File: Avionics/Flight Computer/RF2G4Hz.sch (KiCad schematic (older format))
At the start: 37 parts, among them J5 0734120110, U3 CC2650F128RGZR, U4 CC2592RGVR, Y5 XRCGB24M000F2P00R0

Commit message: Some more pin swapping and routing of signals. Placed reset pullup resistors.
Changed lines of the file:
@@
 $EndComp
 $Comp
-L GND #PWR063
+L GND #PWR76
 U 1 1 58AA6B6F
 P 7100 2700
-F 0 "#PWR063" H 7100 2450 50  0001 C CNN
+F 0 "#PWR76" H 7100 2450 50  0001 C CNN
 F 1 "GND" H 7100 2550 50  0000 C CNN
 F 2 "" H 7100 2700 50  0001 C CNN
@@
 $EndComp
 $Comp
-L GND #PWR064
+L GND #PWR80
 U 1 1 58AA6B99
 P 7900 2700
-F 0 "#PWR064" H 7900 2450 50  0001 C CNN
+F 0 "#PWR80" H 7900 2450 50  0001 C CNN
 F 1 "GND" H 7900 2550 50  0000 C CNN
 F 2 "" H 7900 2700 50  0001 C CNN
@@
 $EndComp
 $Comp
-L GND #PWR065
+L GND #PWR84
 U 1 1 58AA6BBC
 P 8400 2700
-F 0 "#PWR065" H 8400 2450 50  0001 C CNN
+F 0 "#PWR84" H 8400 2450 50  0001 C CNN
 F 1 "GND" H 8400 2550 50  0000 C CNN
 F 2 "" H 8400 2700 50  0001 C CNN
@@
 $EndComp
 $Comp
-L GND #PWR066
+L GND #PWR74
 U 1 1 58AA6BDF
 P 6400 1200
-F 0 "#PWR066" H 6400 950 50  0001 C CNN
+F 0 "#PWR74" H 6400 950 50  0001 C CNN
 F 1 "GND" H 6400 1050 50  0000 C CNN
 F 2 "" H 6400 1200 50  0001 C CNN
@@
 $EndComp
 $Comp
-L GND #PWR067
+L GND #PWR88
 U 1 1 58AA6E83
 P 9750 2500
-F 0 "#PWR067" H 9750 2250 50  0001 C CNN
+F 0 "#PWR88" H 9750 2250 50  0001 C CNN
 F 1 "GND" H 9750 2350 50  0000 C CNN
 F 2 "" H 9750 2500 50  0001 C CNN
@@
 $EndComp
 $Comp
-L GND #PWR068
+L GND #PWR83
 U 1 1 58AB3920
 P 8400 1750
-F 0 "#PWR068" H 8400 1500 50  0001 C CNN
+F 0 "#PWR83" H 8400 1500 50  0001 C CNN
 F 1 "GND" H 8400 1600 50  0000 C CNN
 F 2 "" H 8400 1750 50  0001 C CNN
@@
 RF Shield
 $Comp
-L GND #PWR069
+L GND #PWR75
 U 1 1 58AB48CB
 P 6750 1200
-F 0 "#PWR069" H 6750 950 50  0001 C CNN
+F 0 "#PWR75" H 6750 950 50  0001 C CNN
 F 1 "GND" H 6750 1050 50  0000 C CNN
 F 2 "" H 6750 1200 50  0001 C CNN
@@
 $EndComp
 $Comp
-L GND #PWR070
+L GND #PWR77
 U 1 1 58AB4906
 P 7150 1200
-F 0 "#PWR070" H 7150 950 50  0001 C CNN
+F 0 "#PWR77" H 7150 950 50  0001 C CNN
 F 1 "GND" H 7150 1050 50  0000 C CNN
 F 2 "" H 7150 1200 50  0001 C CNN
@@
 $EndComp
 $Comp
-L GND #PWR071
+L GND #PWR81
 U 1 1 58AB5954
 P 8250 5100
-F 0 "#PWR071" H 8250 4850 50  0001 C CNN
+F 0 "#PWR81" H 8250 4850 50  0001 C CNN
 F 1 "GND" H 8250 4950 50  0000 C CNN
 F 2 "" H 8250 5100 50  0001 C CNN
@@
 VDDS_CC2650
 $Comp
-L GND #PWR072
+L GND #PWR73
 U 1 1 58ABB30E
 P 6100 3250
-F 0 "#PWR072" H 6100 3000 50  0001 C CNN
+F 0 "#PWR73" H 6100 3000 50  0001 C CNN
 F 1 "GND" H 6100 3100 50  0000 C CNN
 F 2 "" H 6100 3250 50  0001 C CNN
@@
 $EndComp
 $Comp
-L GND #PWR073
+L GND #PWR71
 U 1 1 58ABBA52
 P 2850 3000
-F 0 "#PWR073" H 2850 2750 50  0001 C CNN
+F 0 "#PWR71" H 2850 2750 50  0001 C CNN
 F 1 "GND" H 2850 2850 50  0000 C CNN
 F 2 "" H 2850 3000 50  0001 C CNN
@@
 $EndComp
 $Comp
-L GND #PWR074
+L GND #PWR70
 U 1 1 58ABE732
 P 2350 1450
-F 0 "#PWR074" H 2350 1200 50  0001 C CNN
+F 0 "#PWR70" H 2350 1200 50  0001 C CNN
 F 1 "GND" H 2350 1300 50  0000 C CNN
 F 2 "" H 2350 1450 50  0001 C CNN
@@
 CC2650 VDDS Decoupling
 $Comp
-L GND #PWR075
+L GND #PWR85
 U 1 1 58AC3449
 P 9100 6000
-F 0 "#PWR075" H 9100 5750 50  0001 C CNN
+F 0 "#PWR85" H 9100 5750 50  0001 C CNN
 F 1 "GND" H 9100 5850 50  0000 C CNN
 F 2 "" H 9100 6000 50  0001 C CNN
@@
 $EndComp
 $Comp
-L GND #PWR076
+L GND #PWR86
 U 1 1 58AC3569
 P 9400 6000
-F 0 "#PWR076" H 9400 5750 50  0001 C CNN
+F 0 "#PWR86" H 9400 5750 50  0001 C CNN
 F 1 "GND" H 9400 5850 50  0000 C CNN
 F 2 "" H 9400 6000 50  0001 C CNN
@@
 $EndComp
 $Comp
-L GND #PWR077
+L GND #PWR87
 U 1 1 58AC35CB
 P 9700 6000
-F 0 "#PWR077" H 9700 5750 50  0001 C CNN
+F 0 "#PWR87" H 9700 5750 50  0001 C CNN
 F 1 "GND" H 9700 5850 50  0000 C CNN
 F 2 "" H 9700 6000 50  0001 C CNN
@@
 $EndComp
 $Comp
-L GND #PWR078
+L GND #PWR89
 U 1 1 58AC362D
 P 10000 6000
-F 0 "#PWR078" H 10000 5750 50  0001 C CNN
+F 0 "#PWR89" H 10000 5750 50  0001 C CNN
 F 1 "GND" H 10000 5850 50  0000 C CNN
 F 2 "" H 10000 6000 50  0001 C CNN
@@
 $EndComp
 $Comp
-L GND #PWR079
+L GND #PWR90
 U 1 1 58AC368F
 P 10300 6000
-F 0 "#PWR079" H 10300 5750 50  0001 C CNN
+F 0 "#PWR90" H 10300 5750 50  0001 C CNN
 F 1 "GND" H 10300 5850 50  0000 C CNN
 F 2 "" H 10300 6000 50  0001 C CNN
@@
 Pin 34
 $Comp
-L GND #PWR080
+L GND #PWR67
 U 1 1 58AC8629
 P 1400 1450
-F 0 "#PWR080" H 1400 1200 50  0001 C CNN
+F 0 "#PWR67" H 1400 1200 50  0001 C CNN
 F 1 "GND" H 1400 1300 50  0000 C CNN
 F 2 "" H 1400 1450 50  0001 C CNN
@@
 $EndComp
 $Comp
-L GND #PWR081
+L GND #PWR69
 U 1 1 58AC8691
 P 1700 1450
-F 0 "#PWR081" H 1700 1200 50  0001 C CNN
+F 0 "#PWR69" H 1700 1200 50  0001 C CNN
 F 1 "GND" H 1700 1300 50  0000 C CNN
 F 2 "" H 1700 1450 50  0001 C CNN
@@
 VDDR Decoupling
 $Comp
-L GND #PWR082
+L GND #PWR72
 U 1 1 58ACE800
 P 3750 3200
-F 0 "#PWR082" H 3750 2950 50  0001 C CNN
+F 0 "#PWR72" H 3750 2950 50  0001 C CNN
 F 1 "GND" H 3750 3050 50  0000 C CNN
 F 2 "" H 3750 3200 50  0001 C CNN
@@
 $EndComp
 $Comp
-L GND #PWR083
+L GND #PWR82
 U 1 1 58AD6FCF
 P 8250 6000
-F 0 "#PWR083" H 8250 5750 50  0001 C CNN
+F 0 "#PWR82" H 8250 5750 50  0001 C CNN
 F 1 "GND" H 8250 5850 50  0000 C CNN
 F 2 "" H 8250 6000 50  0001 C CNN
@@
 $EndComp
 $Comp
-L +3.3V #PWR084
+L +3.3V #PWR78
 U 1 1 58ABAEB2
 P 7400 4700
-F 0 "#PWR084" H 7450 4750 50  0001 C CNN
+F 0 "#PWR78" H 7450 4750 50  0001 C CNN
 F 1 "+3.3V" H 7415 4873 50  0000 C CNN
 F 2 "" H 50  -100 50  0001 C CNN
@@
 $EndComp
 $Comp
-L +3.3V #PWR085
+L +3.3V #PWR79
 U 1 1 58ABAF0C
 P 7400 5600
-F 0 "#PWR085" H 7450 5650 50  0001 C CNN
+F 0 "#PWR79" H 7450 5650 50  0001 C CNN
 F 1 "+3.3V" H 7415 5773 50  0000 C CNN
 F 2 "" H 50  800 50  0001 C CNN
@@
 $EndComp
 $Comp
-L GND #PWR086
+L GND #PWR68
 U 1 1 58B9D496
 P 1450 3550
-F 0 "#PWR086" H 1450 3300 50  0001 C CNN
+F 0 "#PWR68" H 1450 3300 50  0001 C CNN
 F 1 "GND" H 1450 3400 50  0000 C CNN
 F 2 "" H 1450 3550 50  0001 C CNN
@@
 Text Label 1550 5450 0    60   ~ 0
 ADIO-30
+Text Label 4300 4650 2    60   ~ 0
+PA_EN
 Text Label 4300 4550 2    60   ~ 0
-PA_EN
-Text Label 4300 4650 2    60   ~ 0
 LNA_EN
 Text Label 4300 4950 2    60   ~ 0
@@
 $EndComp
 $Comp
-L GND #PWR087
+L GND #PWR66
 U 1 1 58C28056
 P 1000 2150
-F 0 "#PWR087" H 1050 2200 50  0001 C CNN
+F 0 "#PWR66" H 1050 2200 50  0001 C CNN
 F 1 "GND" H 1005 1977 50  0000 C CNN
 F 2 "" H -5800 -1600 50  0001 C CNN
@@
 $EndComp
 $Comp
-L +3.3V #PWR088
+L +3.3V #PWR65
 U 1 1 58C2A4C4
 P 1000 1450
-F 0 "#PWR088" H 1050 1500 50  0001 C CNN
+F 0 "#PWR65" H 1050 1500 50  0001 C CNN
 F 1 "+3.3V" H 1000 1600 50  0000 C CNN
 F 2 "" H -6350 -3350 50  0001 C CNN

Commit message: Finished routing and DRC check.
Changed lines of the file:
@@
 $EndComp
 $Comp
-L GND #PWR065
+L GND #PWR075
 U 1 1 58AA6B6F
 P 7100 2700
-F 0 "#PWR065" H 7100 2450 50  0001 C CNN
+F 0 "#PWR075" H 7100 2450 50  0001 C CNN
 F 1 "GND" H 7100 2550 50  0000 C CNN
 F 2 "" H 7100 2700 50  0001 C CNN
@@
 $EndComp
 $Comp
-L GND #PWR066
+L GND #PWR076
 U 1 1 58AA6B99
 P 7900 2700
-F 0 "#PWR066" H 7900 2450 50  0001 C CNN
+F 0 "#PWR076" H 7900 2450 50  0001 C CNN
 F 1 "GND" H 7900 2550 50  0000 C CNN
 F 2 "" H 7900 2700 50  0001 C CNN
@@
 $EndComp
 $Comp
-L GND #PWR067
+L GND #PWR077
 U 1 1 58AA6BBC
 P 8400 2700
-F 0 "#PWR067" H 8400 2450 50  0001 C CNN
+F 0 "#PWR077" H 8400 2450 50  0001 C CNN
 F 1 "GND" H 8400 2550 50  0000 C CNN
 F 2 "" H 8400 2700 50  0001 C CNN
@@
 $EndComp
 $Comp
-L GND #PWR068
+L GND #PWR078
 U 1 1 58AA6BDF
 P 6400 1200
-F 0 "#PWR068" H 6400 950 50  0001 C CNN
+F 0 "#PWR078" H 6400 950 50  0001 C CNN
 F 1 "GND" H 6400 1050 50  0000 C CNN
 F 2 "" H 6400 1200 50  0001 C CNN
@@
 $EndComp
 $Comp
-L GND #PWR069
+L GND #PWR079
 U 1 1 58AA6E83
 P 9750 2500
-F 0 "#PWR069" H 9750 2250 50  0001 C CNN
+F 0 "#PWR079" H 9750 2250 50  0001 C CNN
 F 1 "GND" H 9750 2350 50  0000 C CNN
 F 2 "" H 9750 2500 50  0001 C CNN
@@
 $EndComp
 $Comp
-L GND #PWR070
+L GND #PWR080
 U 1 1 58AB3920
 P 8400 1750
-F 0 "#PWR070" H 8400 1500 50  0001 C CNN
+F 0 "#PWR080" H 8400 1500 50  0001 C CNN
 F 1 "GND" H 8400 1600 50  0000 C CNN
 F 2 "" H 8400 1750 50  0001 C CNN
@@
 RF Shield
 $Comp
-L GND #PWR071
+L GND #PWR081
 U 1 1 58AB48CB
 P 6750 1200
-F 0 "#PWR071" H 6750 950 50  0001 C CNN
+F 0 "#PWR081" H 6750 950 50  0001 C CNN
 F 1 "GND" H 6750 1050 50  0000 C CNN
 F 2 "" H 6750 1200 50  0001 C CNN
@@
 $EndComp
 $Comp
-L GND #PWR072
+L GND #PWR082
 U 1 1 58AB4906
 P 7150 1200
-F 0 "#PWR072" H 7150 950 50  0001 C CNN
+F 0 "#PWR082" H 7150 950 50  0001 C CNN
 F 1 "GND" H 7150 1050 50  0000 C CNN
 F 2 "" H 7150 1200 50  0001 C CNN
@@
 $EndComp
 $Comp
-L GND #PWR073
+L GND #PWR083
 U 1 1 58AB5954
 P 8250 5100
-F 0 "#PWR073" H 8250 4850 50  0001 C CNN
+F 0 "#PWR083" H 8250 4850 50  0001 C CNN
 F 1 "GND" H 8250 4950 50  0000 C CNN
 F 2 "" H 8250 5100 50  0001 C CNN
@@
 Text Label 4900 900  0    60   ~ 0
 VDD_CC2592
-Text Label 8550 4700 0    60   ~ 0
+Text Label 8450 4700 0    60   ~ 0
 VDD_CC2592
 Text Notes 7550 5450 0    60   ~ 0
@@
 VDDS_CC2650
 $Comp
-L GND #PWR074
+L GND #PWR084
 U 1 1 58ABB30E
 P 6100 3250
-F 0 "#PWR074" H 6100 3000 50  0001 C CNN
+F 0 "#PWR084" H 6100 3000 50  0001 C CNN
 F 1 "GND" H 6100 3100 50  0000 C CNN
 F 2 "" H 6100 3250 50  0001 C CNN
@@
 $EndComp
 $Comp
-L GND #PWR075
+L GND #PWR085
 U 1 1 58ABBA52
 P 2850 3000
-F 0 "#PWR075" H 2850 2750 50  0001 C CNN
+F 0 "#PWR085" H 2850 2750 50  0001 C CNN
 F 1 "GND" H 2850 2850 50  0000 C CNN
 F 2 "" H 2850 3000 50  0001 C CNN
@@
 $EndComp
 $Comp
-L GND #PWR076
+L GND #PWR086
 U 1 1 58ABE732
 P 2350 1450
-F 0 "#PWR076" H 2350 1200 50  0001 C CNN
+F 0 "#PWR086" H 2350 1200 50  0001 C CNN
 F 1 "GND" H 2350 1300 50  0000 C CNN
 F 2 "" H 2350 1450 50  0001 C CNN
@@
 CC2650 VDDS Decoupling
 $Comp
-L GND #PWR077
+L GND #PWR087
 U 1 1 58AC3449
 P 9100 6000
-F 0 "#PWR077" H 9100 5750 50  0001 C CNN
+F 0 "#PWR087" H 9100 5750 50  0001 C CNN
 F 1 "GND" H 9100 5850 50  0000 C CNN
 F 2 "" H 9100 6000 50  0001 C CNN
@@
 $EndComp
 $Comp
-L GND #PWR078
+L GND #PWR088
 U 1 1 58AC3569
 P 9400 6000
-F 0 "#PWR078" H 9400 5750 50  0001 C CNN
+F 0 "#PWR088" H 9400 5750 50  0001 C CNN
 F 1 "GND" H 9400 5850 50  0000 C CNN
 F 2 "" H 9400 6000 50  0001 C CNN
@@
 $EndComp
 $Comp
-L GND #PWR079
+L GND #PWR089
 U 1 1 58AC35CB
 P 9700 6000
-F 0 "#PWR079" H 9700 5750 50  0001 C CNN
+F 0 "#PWR089" H 9700 5750 50  0001 C CNN
 F 1 "GND" H 9700 5850 50  0000 C CNN
 F 2 "" H 9700 6000 50  0001 C CNN
@@
 $EndComp
 $Comp
-L GND #PWR080
+L GND #PWR090
 U 1 1 58AC362D
 P 10000 6000
-F 0 "#PWR080" H 10000 5750 50  0001 C CNN
+F 0 "#PWR090" H 10000 5750 50  0001 C CNN
 F 1 "GND" H 10000 5850 50  0000 C CNN
 F 2 "" H 10000 6000 50  0001 C CNN
@@
 $EndComp
 $Comp
-L GND #PWR081
+L GND #PWR091
 U 1 1 58AC368F
 P 10300 6000
-F 0 "#PWR081" H 10300 5750 50  0001 C CNN
+F 0 "#PWR091" H 10300 5750 50  0001 C CNN
 F 1 "GND" H 10300 5850 50  0000 C CNN
 F 2 "" H 10300 6000 50  0001 C CNN
@@
 Pin 34
 $Comp
-L GND #PWR082
+L GND #PWR092
 U 1 1 58AC8629
 P 1400 1450
-F 0 "#PWR082" H 1400 1200 50  0001 C CNN
+F 0 "#PWR092" H 1400 1200 50  0001 C CNN
 F 1 "GND" H 1400 1300 50  0000 C CNN
 F 2 "" H 1400 1450 50  0001 C CNN
@@
 $EndComp
 $Comp
-L GND #PWR083
+L GND #PWR093
 U 1 1 58AC8691
 P 1700 1450
-F 0 "#PWR083" H 1700 1200 50  0001 C CNN
+F 0 "#PWR093" H 1700 1200 50  0001 C CNN
 F 1 "GND" H 1700 1300 50  0000 C CNN
 F 2 "" H 1700 1450 50  0001 C CNN
@@
 VDDR Decoupling
 $Comp
-L GND #PWR084
+L GND #PWR094
 U 1 1 58ACE800
 P 3750 3200
-F 0 "#PWR084" H 3750 2950 50  0001 C CNN
+F 0 "#PWR094" H 3750 2950 50  0001 C CNN
 F 1 "GND" H 3750 3050 50  0000 C CNN
 F 2 "" H 3750 3200 50  0001 C CNN
@@
 $EndComp
 $Comp
-L GND #PWR085
+L GND #PWR095
 U 1 1 58AD6FCF
 P 8250 6000
-F 0 "#PWR085" H 8250 5750 50  0001 C CNN
+F 0 "#PWR095" H 8250 5750 50  0001 C CNN
 F 1 "GND" H 8250 5850 50  0000 C CNN
 F 2 "" H 8250 6000 50  0001 C CNN
@@
 $EndComp
 $Comp
-L +3.3V #PWR086
+L +3.3V #PWR096
 U 1 1 58ABAEB2
 P 7400 4700
-F 0 "#PWR086" H 7450 4750 50  0001 C CNN
+F 0 "#PWR096" H 7450 4750 50  0001 C CNN
 F 1 "+3.3V" H 7415 4873 50  0000 C CNN
 F 2 "" H 50  -100 50  0001 C CNN
@@
 $EndComp
 $Comp
-L +3.3V #PWR087
+L +3.3V #PWR097
 U 1 1 58ABAF0C
 P 7400 5600
-F 0 "#PWR087" H 7450 5650 50  0001 C CNN
+F 0 "#PWR097" H 7450 5650 50  0001 C CNN
 F 1 "+3.3V" H 7415 5773 50  0000 C CNN
 F 2 "" H 50  800 50  0001 C CNN
@@
 $EndComp
 $Comp
-L GND #PWR088
+L GND #PWR098
 U 1 1 58B9D496
 P 1450 3550
-F 0 "#PWR088" H 1450 3300 50  0001 C CNN
+F 0 "#PWR098" H 1450 3300 50  0001 C CNN
 F 1 "GND" H 1450 3400 50  0000 C CNN
 F 2 "" H 1450 3550 50  0001 C CNN
@@
 	7400 4700 7600 4700
 Wire Wire Line
-	7900 5600 10300 5600
+	7900 5600 10500 5600
 Wire Wire Line
 	7400 5600 7600 5600
@@
 	1400 1100 2750 1100
 Wire Wire Line
-	2750 1100 2750 1150
+	2750 950  2750 1150
 Wire Wire Line
 	2650 1100 2650 1600
@@
 	2950 1600 2950 1200
 Wire Wire Line
-	2950 1200 3450 1200
+	2950 1200 3250 1200
 Wire Wire Line
 	3250 1200 3250 1600
@@
 	3150 1200 3150 1600
 Connection ~ 3150 1200
-Connection ~ 3250 1200
 Wire Wire Line
 	10300 5600 10300 5700
@@
 $EndComp
 $Comp
-L GND #PWR089
+L GND #PWR099
 U 1 1 58C28056
 P 1000 2150
-F 0 "#PWR089" H 1050 2200 50  0001 C CNN
+F 0 "#PWR099" H 1050 2200 50  0001 C CNN
 F 1 "GND" H 1005 1977 50  0000 C CNN
 F 2 "" H -5800 -1600 50  0001 C CNN
@@
 $EndComp
 $Comp
-L +3.3V #PWR090
+L +3.3V #PWR0100
 U 1 1 58C2A4C4
 P 1000 1450
-F 0 "#PWR090" H 1050 1500 50  0001 C CNN
+F 0 "#PWR0100" H 1050 1500 50  0001 C CNN
 F 1 "+3.3V" H 1000 1600 50  0000 C CNN
 F 2 "" H -6350 -3350 50  0001 C CNN
@@
 Text Label 3950 1650 2    60   ~ 0
 HGM
+Connection ~ 2750 1100
+$Comp
+L PWR_FLAG #FLG0101
+U 1 1 58BEB6A5
+P 9100 4700
+F 0 "#FLG0101" H 4750 3825 50  0001 C CNN
+F 1 "PWR_FLAG" H 9100 4874 50  0000 C CNN
+F 2 "" H 4750 3750 50  0001 C CNN
+F 3 "" H 4750 3750 50  0001 C CNN
+	1    9100 4700
+	1    0    0    -1
+$EndComp
+$Comp
+L PWR_FLAG #FLG0102
+U 1 1 58BEBD3F
+P 10500 5600
+F 0 "#FLG0102" H 6150 4725 50  0001 C CNN
+F 1 "PWR_FLAG" H 10500 5774 50  0000 C CNN
+F 2 "" H 6150 4650 50  0001 C CNN
+F 3 "" H 6150 4650 50  0001 C CNN
+	1    10500 5600
+	1    0    0    -1
+$EndComp
+Connection ~ 10300 5600
+$Comp
+L PWR_FLAG #FLG0103
+U 1 1 58BEAED8
+P 2750 950
+F 0 "#FLG0103" H -1600 75  50  0001 C CNN
+F 1 "PWR_FLAG" H 2750 1124 50  0000 C CNN
+F 2 "" H -1600 0   50  0001 C CNN
+F 3 "" H -1600 0   50  0001 C CNN
+	1    2750 950
+	1    0    0    -1
+$EndComp
 $EndSCHEMATC

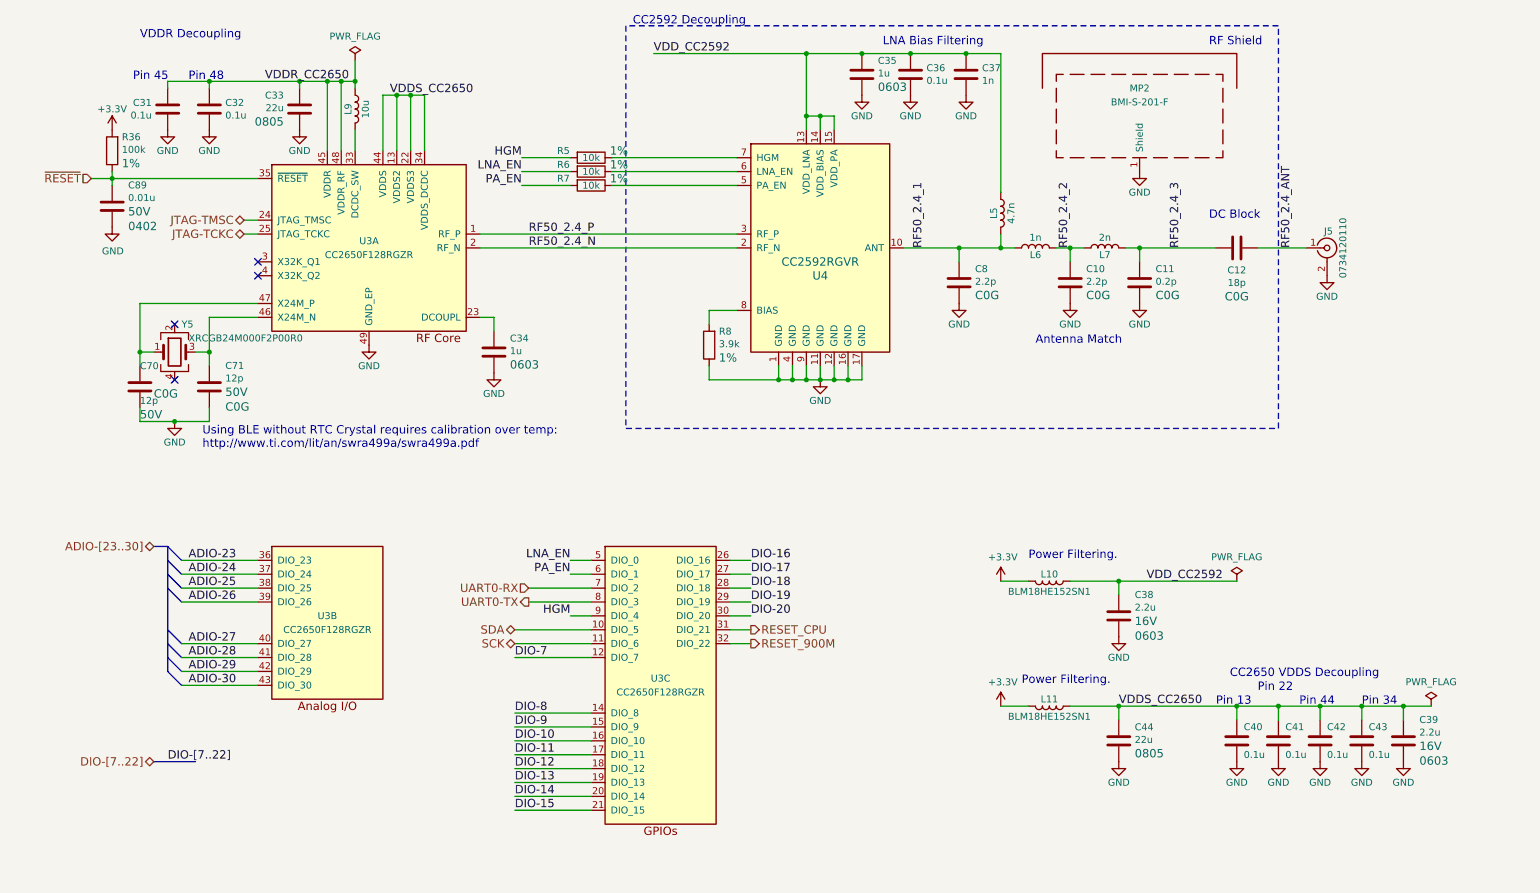
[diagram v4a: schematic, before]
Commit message: Changed LED configuration, added smart driver chip to let all the CPUs access it..
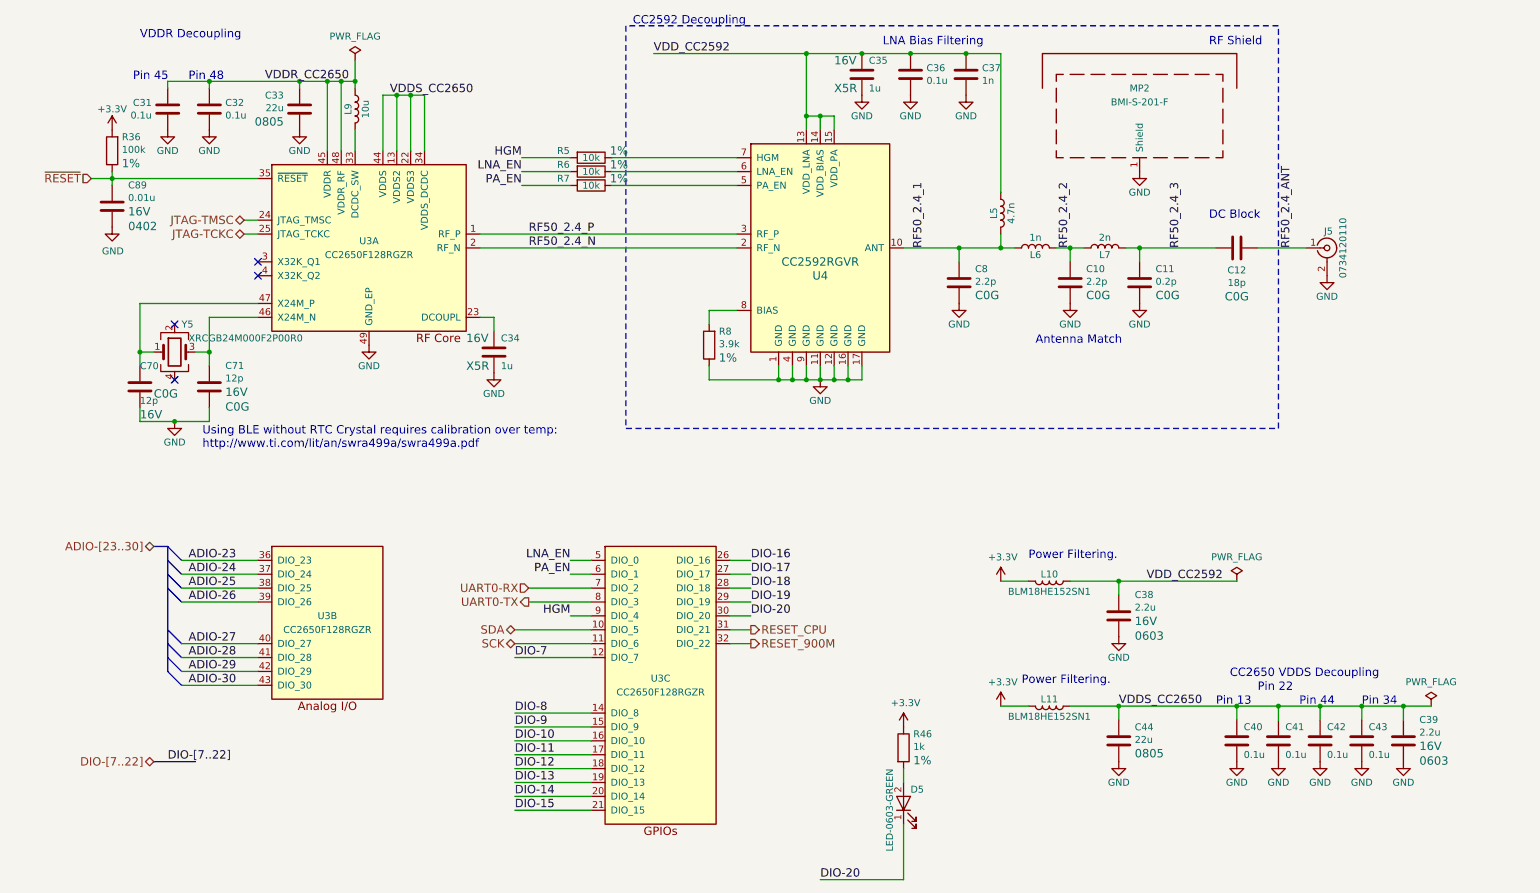
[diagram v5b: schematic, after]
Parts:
- added D5: LED-0603-GREEN, LEDs:LED_0603, symbol LED
- added R46: 1k, Resistors_SMD:R_0402, symbol R
- C10, C11, C12, C31, C32, C36, C37, C40, C41, C42, C43, C70, C71, C8, C89, R36, R5, R6, R7, R8: Voltage 50V -> 16V
- C34, C35: footprint Capacitors_SMD:C_0603 -> Capacitors_SMD:C_0402; Package 0603 -> 0402; Type X7R -> X5R; Voltage 50V -> 16V
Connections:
- wire segments 103 -> 106

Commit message: DFM/BOM Optimizations
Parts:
- J5: value 0734120110 -> 734120110
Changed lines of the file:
@@
 P 9750 2300
 F 0 "J5" H 9760 2420 50  0000 C CNN
-F 1 "0734120110" V 9865 2300 50  0000 C CNN
+F 1 "734120110" V 9865 2300 50  0000 C CNN
 F 2 "Connectors_Molex:Molex_Microcoaxial_RF" H 9750 2300 50  0001 C CNN
 F 3 "http://www.molex.com/pdm_docs/sd/734120110_sd.pdf" H 9750 2300 50  0001 C CNN
